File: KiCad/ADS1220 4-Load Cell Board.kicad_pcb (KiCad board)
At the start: 2 copper layers, 101.6 x 50.8 mm, 84 parts, among them J1 Conn_01x04, J2 Conn_01x04, J3 Conn_01x04, J5 USB_C_Receptacle_USB2.0_14P, J6 Conn_01x02, J7 Conn_01x04, SW1 SW_Push, SW2 SW_Push, U1 STM32F103C8Tx, U2 ADS1220xPW, U3 MCP6V92-E/MS, U4 NCP1117-3.3_SOT223, U5 XPS62912RPUR, Y1 8Mhz

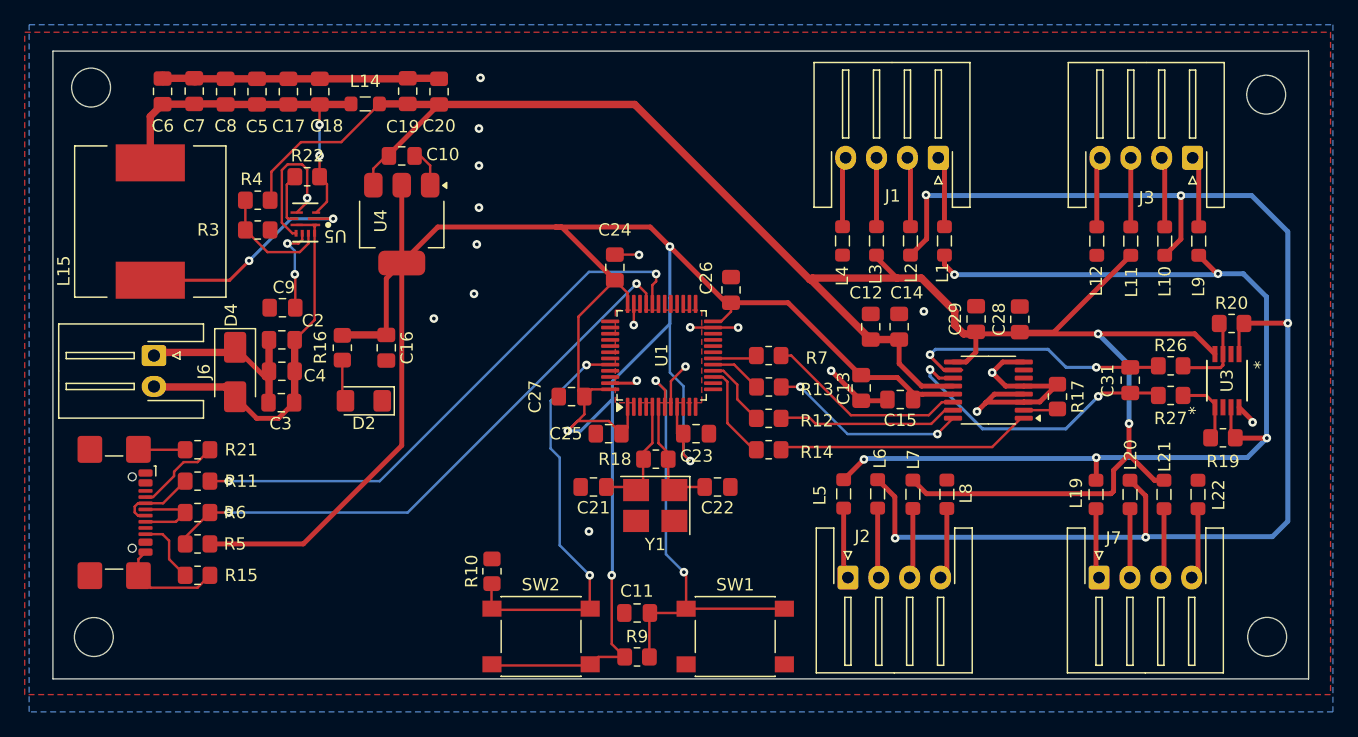
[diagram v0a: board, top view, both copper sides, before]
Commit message: Update USB Connector
Update USB connector and design rules so it passes inspection.
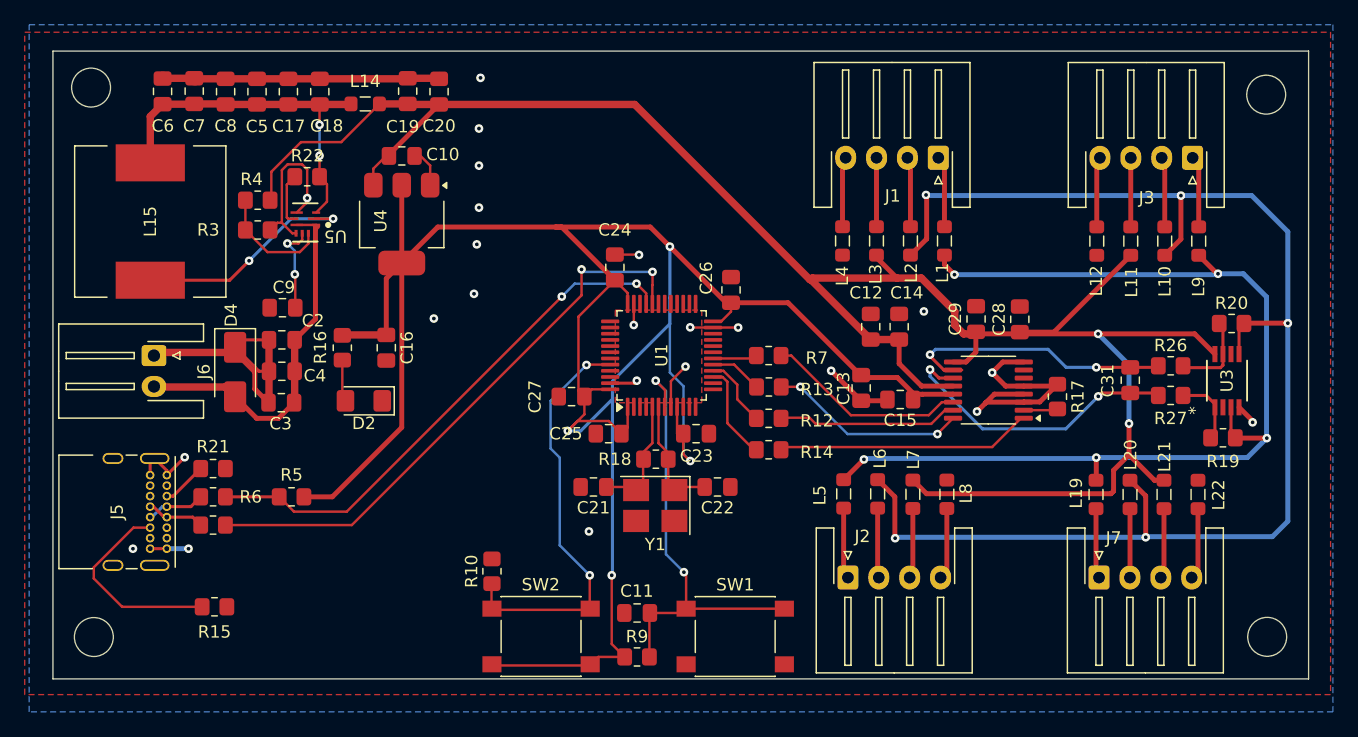
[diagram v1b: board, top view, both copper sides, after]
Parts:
- J5: footprint Connector_USB:USB_C_Receptacle_GCT_USB4110 -> Connector_USB:USB_C_Receptacle_GCT_USB4085
- moved R5 8.51 mm to (56.1, 104.9)
- moved J5 6.19 mm to (46.0, 103.1)
- moved R11 3.77 mm to (49.8, 107.2)
- moved R15 2.89 mm to (49.9, 113.8)
- moved R21 1.97 mm to (49.8, 102.6), turned to 180 degrees
- moved R6 1.78 mm to (49.8, 104.9)
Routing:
- net Net-(J5-CC2): track 5.46 -> 16.5 mm
- net +3.3V: track 207.5 -> 197.5 mm
- net USBDP: track 47.5 -> 43.4 mm
- net GND: track 111.2 -> 115.1 mm, vias 20 -> 23
- net Net-(J5-CC1): track 7.00 -> 3.66 mm
- net Net-(J5-D+-PadA6): track 6.83 -> 4.77 mm
- net Net-(J5-D--PadA7): track 6.39 -> 4.71 mm
- net USBDM: track 45.7 -> 47.0 mm
- net +12V: track 31.0 -> 31.6 mm

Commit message: Update Switch Footprints
Update switch schematic and footprint to match the actual part being used
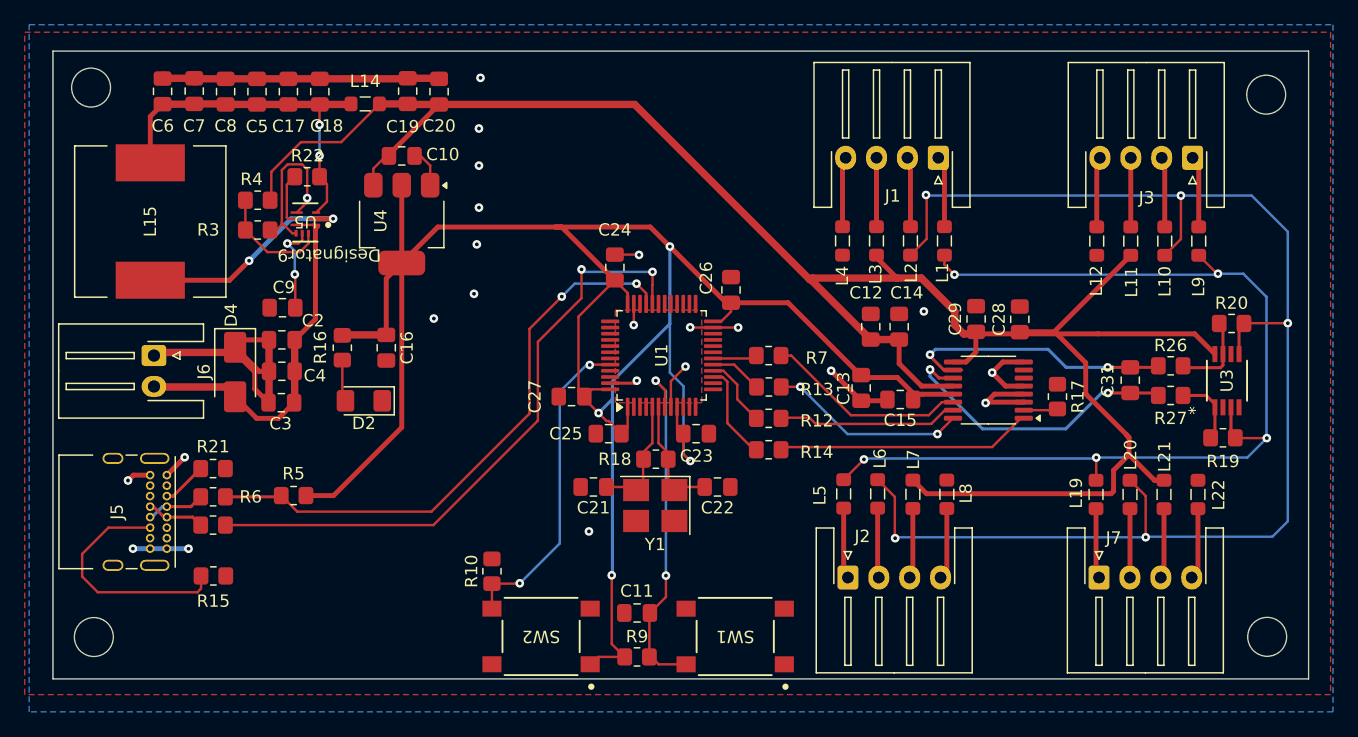
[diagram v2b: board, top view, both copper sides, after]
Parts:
- SW1, SW2: footprint Button_Switch_SMD:SW_Push_1P1T_NO_6x6mm_H9.5mm -> PTS645 Switch:SWITCH_43SMTR92LFS
- moved R15 2.50 mm to (49.8, 111.3)
- moved R5 0.19 mm to (56.3, 104.8)
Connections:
- SW1 pad 1: GND -> unconnected-(SW1-Pad1)
- SW2 pad 2: BOOT0_SWCLK -> unconnected-(SW2-Pad2)
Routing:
- net +3.3V: track 197.5 -> 182.2 mm
- net GND: track 115.1 -> 106.7 mm
- net BOOT0_SWCLK: track 34.5 -> 26.6 mm
- net NRESET: track 36.5 -> 28.9 mm
- net +5V: track 168.8 -> 173.3 mm, vias 2 -> 0
- net USBDP: track 43.4 -> 47.7 mm
- net USBDM: track 47.0 -> 50.9 mm
- net Net-(J5-CC2): track 16.5 -> 19.5 mm

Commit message: Update Crystal
Change crystal footprint to ABM3-8.000MHZ-B4Y-T
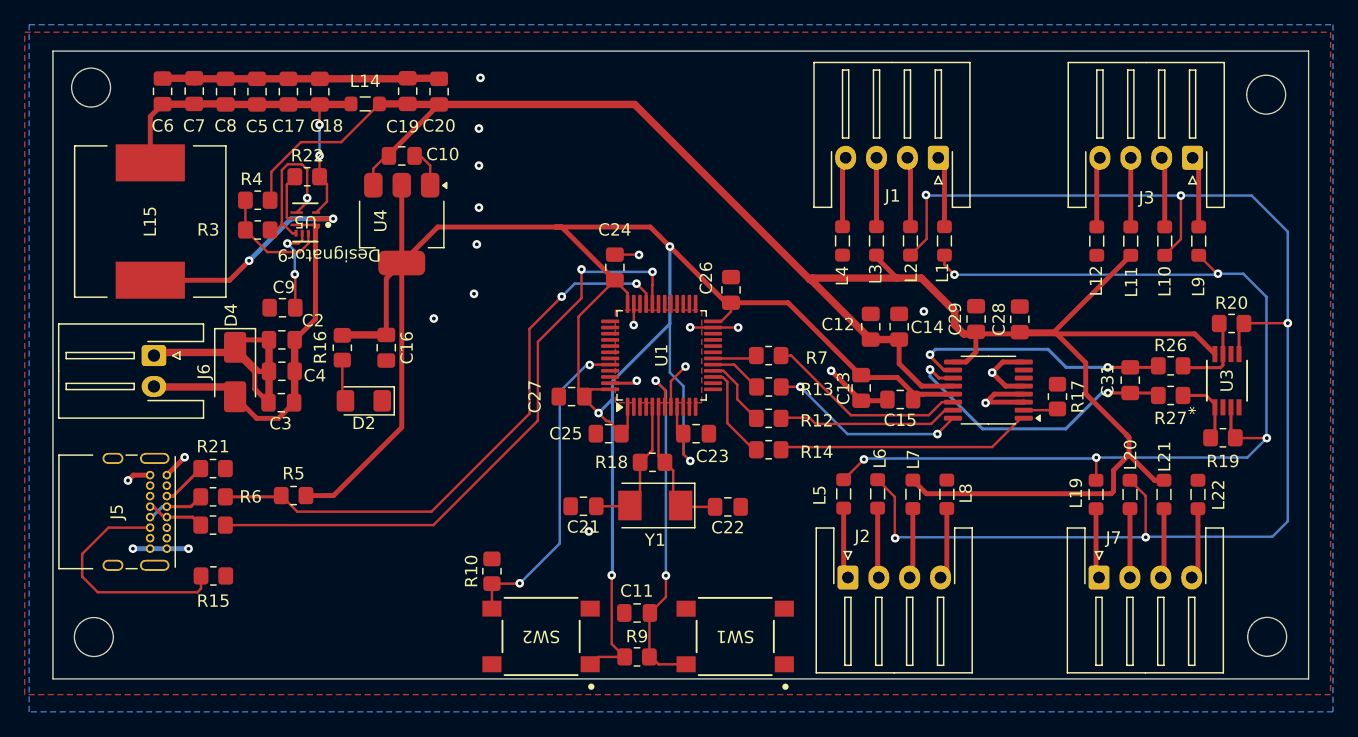
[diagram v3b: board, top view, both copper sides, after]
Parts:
- Y1: footprint Crystal:Crystal_SMD_SeikoEpson_FA238V-4Pin_3.2x2.5mm_HandSoldering -> Crystal:Crystal_SMD_Abracon_ABM3-2Pin_5.0x3.2mm
- moved C22 1.82 mm to (91.4, 105.7)
- moved C21 1.76 mm to (79.8, 105.7)
- moved R18 0.37 mm to (85.3, 102.1)
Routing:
- net GND: track 106.7 -> 103.2 mm
- net PF1: track 9.82 -> 11.6 mm
- net +12V: track 31.6 -> 30.5 mm
- net PF0: track 10.4 -> 11.5 mm
- net Net-(U2-AIN1): track 22.5 -> 21.8 mm
- net +5V: track 173.3 -> 172.6 mm
- net Net-(U2-~{CS}): track 2.79 -> 2.26 mm

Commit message: Update Inductor Footprint
Update to PA4332.222NLT
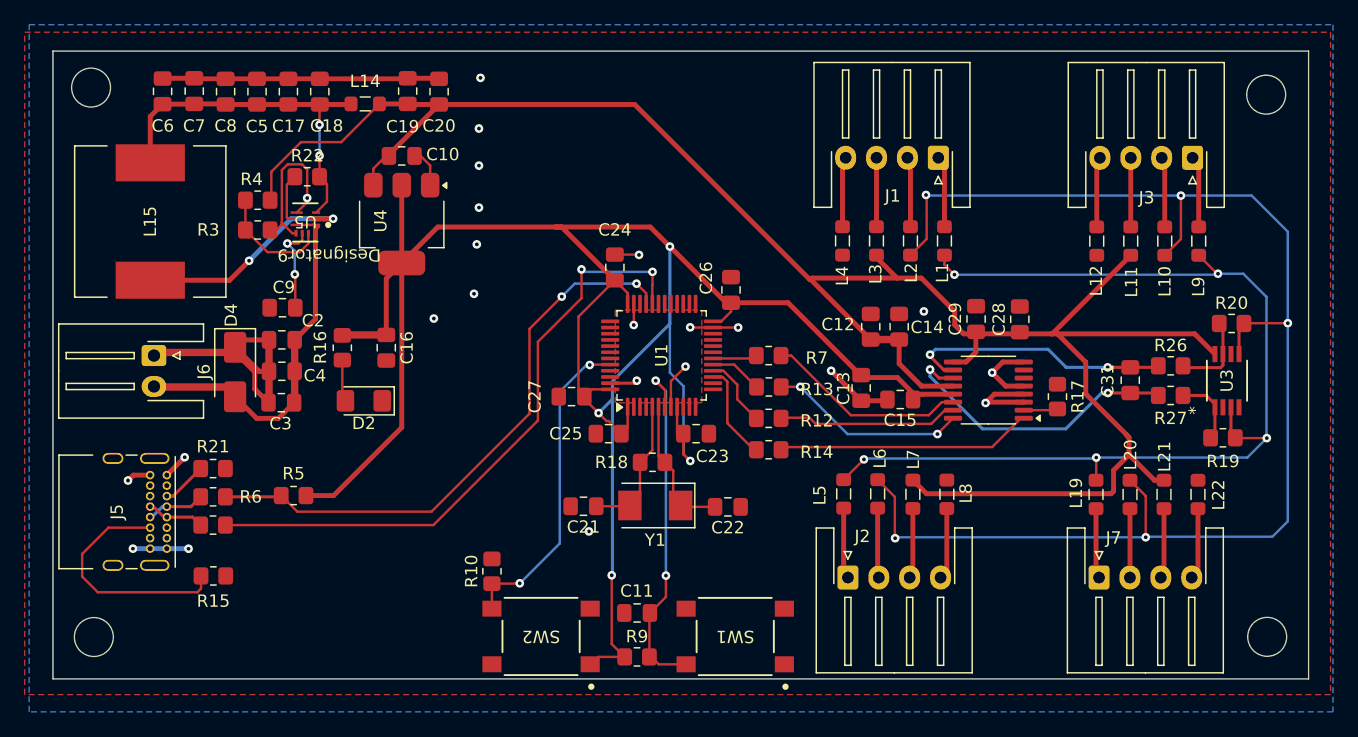
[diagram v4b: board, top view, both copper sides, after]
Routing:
- net +5V: track 172.6 -> 167.2 mm
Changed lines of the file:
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@@
 		(start 65.489 71.077)
 		(end 65.532 71.034)
-		(width 0.6)
+		(width 0.4)
 		(layer "F.Cu")
 		(net 1)
@@
 		(start 65.532 71.034)
 		(end 68.029 71.034)
-		(width 0.6)
+		(width 0.4)
 		(layer "F.Cu")
 		(net 1)
@@
 		(start 68.072 71.077)
 		(end 68.061 71.066)
-		(width 1.1)
+		(width 0.4)
 		(layer "F.Cu")
 		(net 1)
@@
 		(start 53.34 71.077)
 		(end 50.8 71.077)
-		(width 0.6)
+		(width 0.4)
 		(layer "F.Cu")
 		(net 1)
@@
 		(start 58.42 71.077)
 		(end 65.489 71.077)
-		(width 0.6)
+		(width 0.4)
 		(layer "F.Cu")
 		(net 1)
@@
 		(start 48.26 71.034)
 		(end 45.72 71.034)
-		(width 0.6)
+		(width 0.4)
 		(layer "F.Cu")
 		(net 1)
@@
 		(start 45.72 71.034)
 		(end 45.6985 71.0555)
-		(width 1.1)
+		(width 0.4)
 		(layer "F.Cu")
 		(net 1)
@@
 		(start 50.8 71.077)
 		(end 48.303 71.077)
-		(width 0.6)
+		(width 0.4)
 		(layer "F.Cu")
 		(net 1)
@@
 		(start 58.42 71.077)
 		(end 55.88 71.077)
-		(width 0.6)
+		(width 0.4)
 		(layer "F.Cu")
 		(net 1)
@@
 		(start 48.303 71.077)
 		(end 48.26 71.034)
-		(width 1.1)
+		(width 0.4)
 		(layer "F.Cu")
 		(net 1)
@@
 		(start 68.029 71.034)
 		(end 68.072 71.077)
-		(width 0.6)
+		(width 0.4)
 		(layer "F.Cu")
 		(net 1)
@@
 		(start 55.88 71.077)
 		(end 53.34 71.077)
-		(width 0.6)
+		(width 0.4)
 		(layer "F.Cu")
 		(net 1)
@@
 		(start 48.2385 73.1305)
 		(end 48.26 73.109)
-		(width 0.6)
+		(width 0.4)
 		(layer "F.Cu")
 		(net 21)
@@
 		(start 45.6985 73.1305)
 		(end 48.2385 73.1305)
-		(width 0.6)
+		(width 0.4)
 		(layer "F.Cu")
 		(net 21)
@@
 		(start 50.757 73.109)
 		(end 50.8 73.152)
-		(width 0.6)
+		(width 0.4)
 		(layer "F.Cu")
 		(net 21)
@@
 		(start 58.4 73.172)
 		(end 58.42 73.152)
-		(width 0.2)
+		(width 0.4)
 		(layer "F.Cu")
 		(net 21)
@@
 		(start 48.26 73.109)
 		(end 50.757 73.109)
-		(width 0.6)
+		(width 0.4)
 		(layer "F.Cu")
 		(net 21)
@@
 		(start 53.34 73.152)
 		(end 55.88 73.152)
-		(width 0.6)
+		(width 0.4)
 		(layer "F.Cu")
 		(net 21)
@@
 		(start 58.42 73.152)
 		(end 60.903 73.152)
-		(width 0.6)
+		(width 0.4)
 		(layer "F.Cu")
 		(net 21)
@@
 		(start 55.88 73.152)
 		(end 58.42 73.152)
-		(width 0.6)
+		(width 0.4)
 		(layer "F.Cu")
 		(net 21)
@@
 		(start 60.903 73.152)
 		(end 60.946 73.109)
-		(width 0.6)
+		(width 0.4)
 		(layer "F.Cu")
 		(net 21)
@@
 		(start 50.8 73.152)
 		(end 53.34 73.152)
-		(width 0.6)
+		(width 0.4)
 		(layer "F.Cu")
 		(net 21)
@@
 	)
 	(segment
-		(start 123.7234 99.9236)
-		(end 123.7234 99.8982)
+		(start 64.015 77.209)
+		(end 64.015 77.3175)
 		(width 0.4)
 		(layer "F.Cu")
@@
 	)
 	(segment
-		(start 64.015 77.209)
-		(end 64.015 77.3175)
+		(start 123.9 101.5)
+		(end 123.9 100.1002)
 		(width 0.4)
 		(layer "F.Cu")
@@
 		(start 98.15 87.325)
 		(end 98.275 87.2)
-		(width 0.6)
+		(width 0.4)
 		(layer "F.Cu")
 		(net 51)
@@
 		(start 98.275 87.2)
 		(end 105.125 87.2)
-		(width 0.6)
+		(width 0.4)
 		(layer "F.Cu")
 		(net 51)
@@
 	)
 	(segment
-		(start 120.396 94.0562)
-		(end 117.9148 91.575)
-		(width 0.4)
-		(layer "F.Cu")
-		(net 51)
-	)
-	(segment
 		(start 62.7525 78.3475)
 		(end 62.7525 79.6835)
@@
 		(start 109.8 89.9)
 		(end 109.8 91)
-		(width 0.6)
+		(width 0.4)
 		(layer "F.Cu")
 		(net 51)
@@
 	)
 	(segment
-		(start 123.9 101.5)
-		(end 123.9 100.1002)
-		(width 0.4)
-		(layer "F.Cu")
-		(net 51)
-	)
-	(segment
 		(start 105.125 87.2)
 		(end 107.1 87.2)
-		(width 0.6)
-		(layer "F.Cu")
-		(net 51)
-	)
-	(segment
-		(start 123.9 100.1002)
-		(end 123.7234 99.9236)
 		(width 0.4)
 		(layer "F.Cu")
@@
 	)
 	(segment
+		(start 123.9 100.1002)
+		(end 123.7234 99.9236)
+		(width 0.4)
+		(layer "F.Cu")
+		(net 51)
+	)
+	(segment
 		(start 63.246 73.109)
 		(end 65.532 73.109)
-		(width 0.6)
+		(width 0.4)
 		(layer "F.Cu")
 		(net 51)
 	)
 	(segment
-		(start 117.823 91.575)
-		(end 124.04 85.358)
+		(start 117.602 91.7155)
+		(end 117.6825 91.7155)
 		(width 0.4)
 		(layer "F.Cu")
@@
 	)
 	(segment
+		(start 120.396 96.5708)
+		(end 120.396 94.0015)
+		(width 0.4)
+		(layer "F.Cu")
+		(net 51)
+	)
+	(segment
 		(start 110.709 93.991)
 		(end 109.6595 93.991)
@@
 	)
 	(segment
-		(start 109.8 91)
-		(end 110.5155 91.7155)
-		(width 0.6)
+		(start 117.9695 91.575)
+		(end 117.9148 91.575)
+		(width 0.4)
 		(layer "F.Cu")
 		(net 51)
 	)
 	(segment
-		(start 122.65 104.441166)
-		(end 122.441166 104.65)
+		(start 109.8 91)
+		(end 110.5155 91.7155)
 		(width 0.4)
 		(layer "F.Cu")
@@
 	)
 	(segment
-		(start 123.7234 99.8982)
-		(end 120.396 96.5708)
+		(start 122.65 104.441166)
+		(end 122.441166 104.65)
 		(width 0.4)
 		(layer "F.Cu")
@@
 	)
 	(segment
-		(start 117.9148 91.575)
-		(end 115.062 91.575)
-		(width 0.4)
-		(layer "F.Cu")
-		(net 51)
-	)
-	(segment
 		(start 122.65 102.75)
 		(end 122.65 104.441166)
@@
 	)
 	(segment
-		(start 120.396 96.5708)
-		(end 120.396 94.0562)
-		(width 0.4)
-		(layer "F.Cu")
-		(net 51)
-	)
-	(segment
 		(start 83.902 73.152)
 		(end 98.075 87.325)
-		(width 0.6)
+		(width 0.4)
 		(layer "F.Cu")
 		(net 51)
@@
 		(start 98.15 87.325)
 		(end 103 92.175)
-		(width 0.6)
+		(width 0.4)
 		(layer "F.Cu")
 		(net 51)
@@
 	)
 	(segment
-		(start 115.062 91.575)
-		(end 117.823 91.575)
-		(width 0.4)
-		(layer "F.Cu")
-		(net 51)
-	)
-	(segment
 		(start 125.96 103.56)
 		(end 123.9 101.5)
@@
 		(start 107.1 87.2)
 		(end 109.8 89.9)
-		(width 0.6)
+		(width 0.4)
 		(layer "F.Cu")
 		(net 51)
@@
 		(start 68.072 73.152)
 		(end 83.902 73.152)
-		(width 0.6)
+		(width 0.4)
 		(layer "F.Cu")
 		(net 51)
@@
 		(start 110.5155 91.7155)
 		(end 111.506 91.7155)
-		(width 0.6)
+		(width 0.4)
 		(layer "F.Cu")
 		(net 51)
@@
 	)
 	(segment
+		(start 120.396 94.0015)
+		(end 117.9695 91.575)
+		(width 0.4)
+		(layer "F.Cu")
+		(net 51)
+	)
+	(segment
 		(start 107.117 95.941)
 		(end 109.6595 95.941)
@@
 	)
 	(segment
+		(start 117.6825 91.7155)
+		(end 124.04 85.358)
+		(width 0.4)
+		(layer "F.Cu")
+		(net 51)
+	)
+	(segment
 		(start 98.075 87.325)
 		(end 98.15 87.325)
-		(width 0.6)
+		(width 0.4)
 		(layer "F.Cu")
 		(net 51)
@@
 		(start 68.072 73.152)
 		(end 65.575 73.152)
-		(width 0.6)
+		(width 0.4)
+		(layer "F.Cu")
+		(net 51)
+	)
+	(segment
+		(start 123.7234 99.8982)
+		(end 120.396 96.5708)
+		(width 0.4)
 		(layer "F.Cu")
 		(net 51)
@@
 		(layer "F.Cu")
 		(net 51)
+	)
+	(segment
+		(start 123.7234 99.9236)
+		(end 123.7234 99.8982)
+		(width 0.4)
+		(layer "F.Cu")
+		(net 51)
